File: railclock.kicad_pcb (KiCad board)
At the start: 4 copper layers, 99.6 x 99.9 mm, 180 parts, among them J1 Conn_01x02_Pin, J10 Conn_01x04_MountingPin, J11 Conn_01x04_MountingPin, J12 Conn_01x04_MountingPin, J13 Conn_01x04_MountingPin, J14 Conn_01x04_MountingPin, J15 Conn_01x03_MountingPin, J16 Barrel_Jack_Switch, J2 Conn_01x03_MountingPin, J3 Conn_01x04_MountingPin, J4 USB_C_Receptacle_USB2.0_14P, J5 Conn_01x03_MountingPin, J6 Conn_01x03_MountingPin, J7 Conn_01x03_MountingPin, J8 Conn_01x03_MountingPin, J9 Conn_01x04_MountingPin, Q1 Q_NPN_BEC, SW1 SW_SPST, SW2 SW_DPDT_x2, SW3 SW_SPST, U1 MCP7940N-xST, U10 74AHC1G04, U11 MAX811TEUS-T, U12 MCP4728, U13 BTS5012SDA, U14 BTS5012SDA, U15 BTS5012SDA, U16 BTS5012SDA, U17 BTS5012SDA, U2 MCP73832-2-OT, U4 ESP32-C6-WROOM-1, U5 DRV8870DDA, U6 PAM2421, U8 BQ24296MRGET, U9 PCF8574RGTR, Y1 MC-306_32.7680K-A5__ROHS

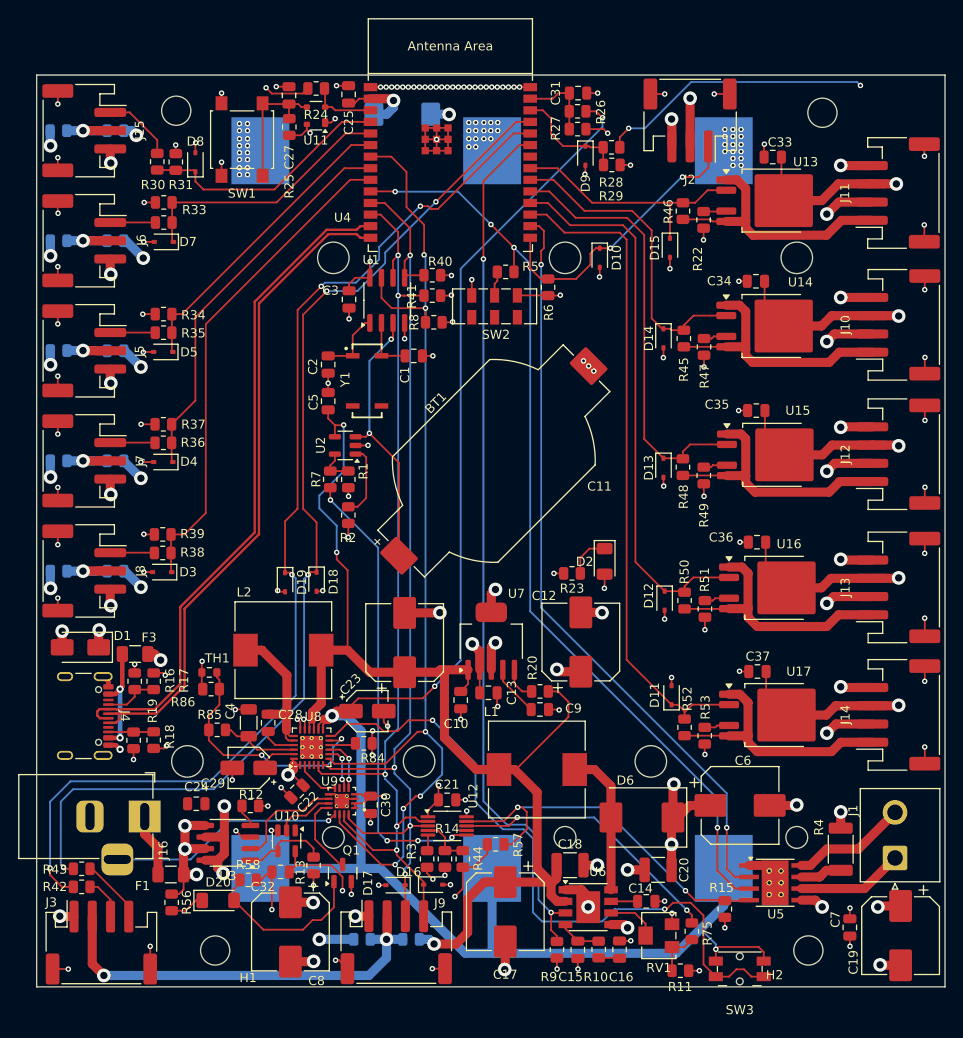
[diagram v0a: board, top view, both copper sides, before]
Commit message: Change charger
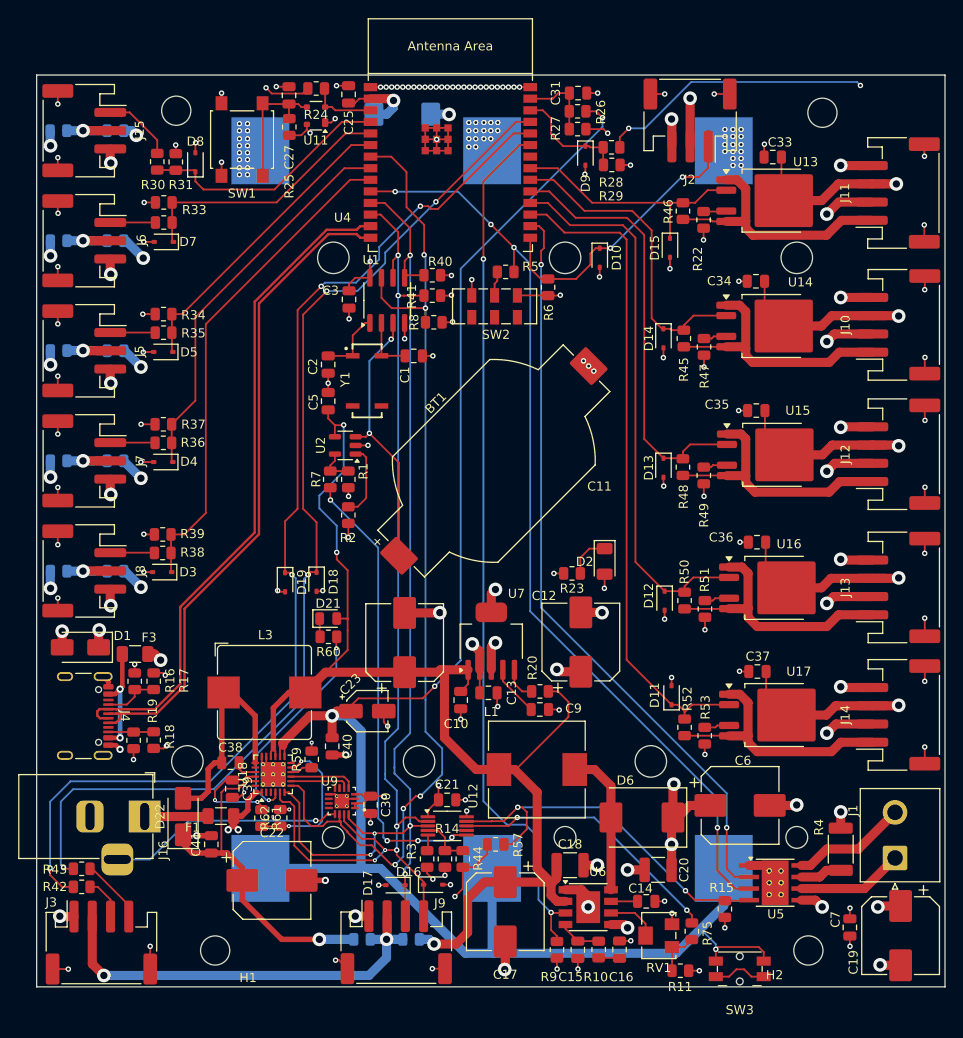
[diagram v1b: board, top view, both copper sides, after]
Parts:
- removed C24, C32: C, Capacitor_SMD:C_0805_2012Metric
- removed C28: 47nF, Capacitor_SMD:C_0805_2012Metric
- removed C29: 8.2uF, Capacitor_SMD:CP_Elec_4x5.3
- removed C4: 4.7uF, Capacitor_SMD:C_1206_3216Metric
- removed C8: C_Polarized, Capacitor_SMD:CP_Elec_8x10
- removed D20: BZV55B7V5, Diode_SMD:D_MiniMELF
- removed L2: L, Inductor_SMD:L_10.4x10.4_H4.8
- removed Q1: Q_NPN_BEC, Package_TO_SOT_SMD:SOT-23
- removed R12: 100R, Resistor_SMD:R_0805_2012Metric
- removed R13: 10K, Resistor_SMD:R_0805_2012Metric
- removed R56, R58, R84: R, Resistor_SMD:R_0805_2012Metric
- removed R85: 5.25K, Resistor_SMD:R_0805_2012Metric
- removed R86: 31.23K, Resistor_SMD:R_0805_2012Metric
- removed TH1: Thermistor_NTC, Resistor_SMD:R_0603_1608Metric
- removed U10: 74AHC1G04, Package_TO_SOT_SMD:SOT-23-5
- removed U3: ~, Package_SO:SOIC-8_3.9x4.9mm_P1.27mm
- removed U8: BQ24296MRGET, Package_DFN_QFN:VQFN-24-1EP_4x4mm_P0.5mm_EP2.5x2.5mm_ThermalVias
- added C38: 100nF, Capacitor_SMD:C_0805_2012Metric, F.Cu at (65.9, 99.0)
- added C39: 4.7uF, Capacitor_SMD:C_0805_2012Metric, F.Cu at (66.2, 101.9)
- added C40: 10uF, Capacitor_SMD:C_0805_2012Metric, F.Cu at (77.1, 97.2)
- added C41: 50uF, Capacitor_SMD:C_0805_2012Metric, F.Cu at (63.9, 108.0)
- added D21: LED, LED_SMD:LED_0805_2012Metric, F.Cu at (76.7, 83.2)
- added D22: SS14-DC, Diode_SMD:D_SMA, F.Cu at (60.8, 104.9)
- added L3: 2.2uF, Inductor_SMD:L_Bourns_SRP1038C_10.0x10.0mm, F.Cu at (69.7, 91.3)
- added R59: R, Resistor_SMD:R_0805_2012Metric, F.Cu at (74.8, 98.6)
- added R60: R, Resistor_SMD:R_0805_2012Metric, F.Cu at (76.7, 85.2)
- added R61: 10k, Resistor_SMD:R_0805_2012Metric, F.Cu at (69.3, 105.1)
- added R62: 10k, Resistor_SMD:R_0805_2012Metric, F.Cu at (71.4, 105.0)
- added U18: BQ25895RTW, Package_DFN_QFN:Texas_RTW_WQFN-24-1EP_4x4mm_P0.5mm_EP2.7x2.7mm_ThermalVias, F.Cu at (70.6, 100.3)
- C22: value C -> C_Polarized; footprint Capacitor_SMD:C_0805_2012Metric -> Capacitor_SMD:CP_Elec_8x10
- moved C22 10.1 mm to (70.5, 111.9), turned to 0 degrees
- moved F1 8.44 mm to (64.9, 104.8)
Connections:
- U9 pad 12: Net-(Q1-C) -> unconnected-(U9-P6-Pad12)
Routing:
- net WAKEUP: track 73.4 -> 5.91 mm, vias 2 -> 0
- net Net-(U8-TS): track 27.2 -> 0.00 mm, vias 2 -> 0
- net Net-(D22-A): track 0.00 -> 25.3 mm
- net Net-(U18-STAT): track 0.00 -> 23.7 mm, vias 0 -> 2
- net Net-(D20-A): track 18.6 -> 0.00 mm
- net GND: track 262.8 -> 245.4 mm, vias 211 -> 202
- net Net-(U18-TS): track 0.00 -> 16.4 mm, vias 0 -> 2
- net Net-(U8-SW_19): track 16.3 -> 0.00 mm
- net +5V: track 31.2 -> 45.6 mm, vias 10 -> 6
- net +12V: track 144.5 -> 131.0 mm
- net VBUS_FLG: track 12.2 -> 0.00 mm
- net Net-(U18-REGN): track 0.00 -> 11.8 mm, vias 0 -> 2
- net +3.3V: track 116.3 -> 105.5 mm, vias 28 -> 27
- net SCL: track 106.6 -> 116.6 mm, vias 5 -> 6
- net Net-(U3-~{EN}): track 9.58 -> 0.00 mm
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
